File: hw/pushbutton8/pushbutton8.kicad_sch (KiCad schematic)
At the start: 34 parts, among them U1 74HC595

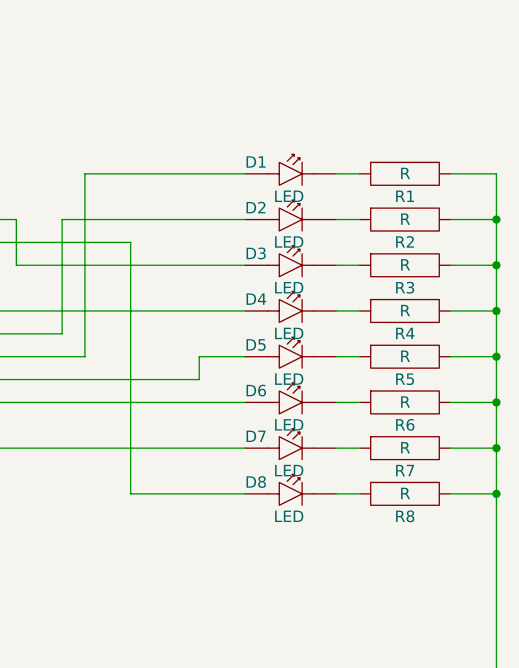
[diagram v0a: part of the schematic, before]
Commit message: pushbutton8 rev.3: Curved slotted holes and enhanced circuit track routing.
This variant has been prototyped at home and tested successfully in Nov. 2023.
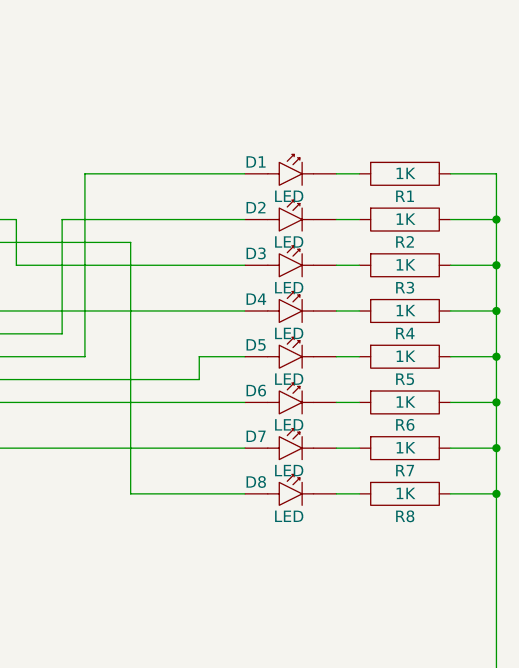
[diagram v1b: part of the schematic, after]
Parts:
- C1, C2: footprint Capacitors_SMD:C_0805 -> Capacitor_SMD:C_0805_2012Metric_Pad1.18x1.45mm_HandSolder
- D1, D2, D3, D4, D5, D6, D7, D8: footprint Resistor:R_0805 -> LED_SMD:LED_0805_2012Metric_Pad1.15x1.40mm_HandSolder
- H5: footprint Mechanical:HOLE_2.5mm -> MountingHole:MountingHole_2.5mm
- R1, R2, R3, R4, R5, R6, R7, R8: value R -> 1K; footprint Resistor:R_0805 -> Resistor_SMD:R_0805_2012Metric_Pad1.20x1.40mm_HandSolder
- R9: footprint Resistor:R_0805 -> Resistor_SMD:R_0805_2012Metric_Pad1.20x1.40mm_HandSolder
